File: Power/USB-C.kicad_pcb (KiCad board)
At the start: 2 copper layers, 80 x 30 mm, 40 parts, among them J1 USB_C_Receptacle_PowerOnly_6P, J2 Barrel_Jack_Switch, J3 Barrel_Jack_Switch, J4 Barrel_Jack_Switch, J5 Barrel_Jack_Switch, SW1 15v12, SW2 12v9, U1 HUSB237, U2 TPS73801, U3 TPS73801

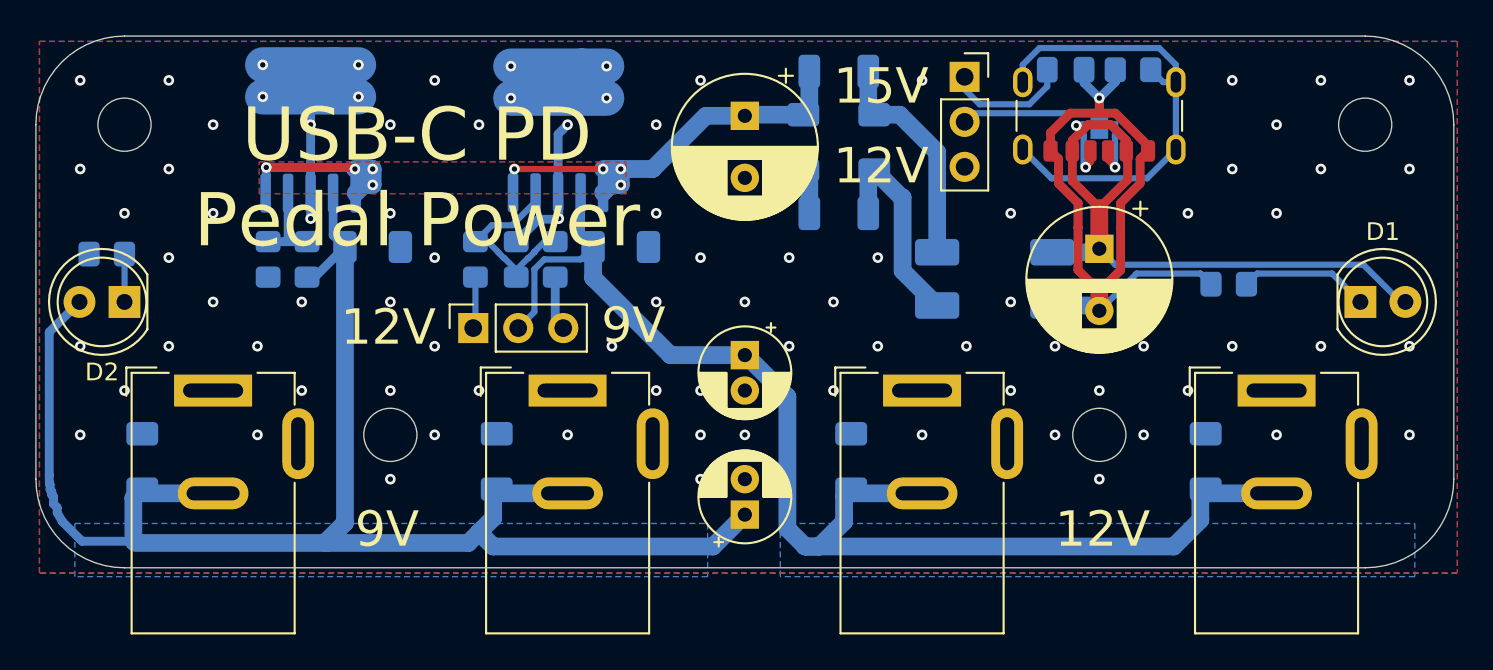
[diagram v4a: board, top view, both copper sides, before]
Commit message: USB-C power board: use the Würth reverse-mounted LEDs
This is the other board that had status lights on the non-SMD side.
Replace the through-hole LED with the reverse-mounted SMD ones.

Signed-off-by: Linus Torvalds <torvalds@linux-foundation.org>
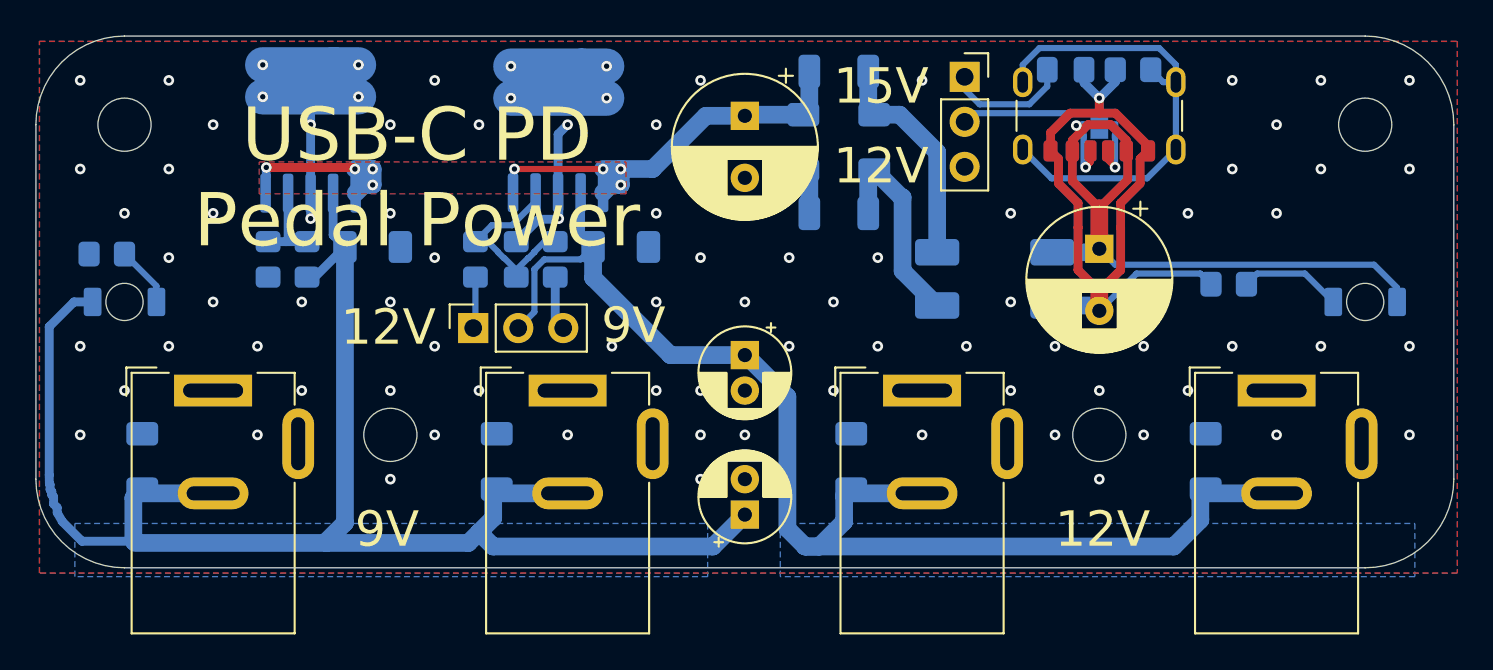
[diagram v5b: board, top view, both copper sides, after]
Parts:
- D1, D2: footprint LED_THT:LED_D5.0mm -> Mylib:Würth Reverse Mount LED; moved to B.Cu
- moved D1 0.27 mm to (125.0, 65.0)
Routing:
- net Net-(D1-K): track 7.34 -> 5.81 mm
- net +9V: track 90.4 -> 91.3 mm
- net Net-(D2-K): track 2.70 -> 3.45 mm

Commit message: Power board: move common mode choke to front
I don't do the nice 3D models, because I'm lazy and it's too much of a
hassle.  But it also means that it wasn't visually obvious that the
common mode choke ends up being very inconvenient on the back of the
board.

I'm perfectly fine with the usual low profile SMD components there, but
that choke is 3.5mm high, which is about twice as much as the other
components.

It's not that bad on the power board (which I don't have an enclosure
for anyway, although I'm looking at maybe just encasing it in resin with
a mold).  On the VGND effects board it's a non-starter.

Of course, I'm not convinced the choke actually matters, and the answer
may just be to remove it again, but until I see the effects of it let's
just move it to the front of the board.

It's going to be inconvenient to solder - I much prefer the hotplate -
but particularly on the power board I already have that USB-C connector
that I do with a hot-air station, and they are right next to each other,
so I can probably just do them together.

I'll have to think about the effects board more.  I don't actually have
room on the top of the board because I want to keep the electrolytics up
there, and keep the area in the middle clear for if I ever re-introduce
the joiner/splitter model with a third audio jack.

I think the inter-board connector there in the middle was a mistake.
It's in the way not only for this choke, but for any single-pot design
if I ever do one.

So the solution may be that I'll just have to move the connector around,
but that obviously means that I lose backwards compatibility with
existing effects boards.  Not really a big deal - unlike the enclosure
changes, it's easy enough to just do new boards - but if I make that
kind of change I want to make sure I think it through and get it right.

So let's wait to see if the choke even makes a difference.

Signed-off-by: Linus Torvalds <torvalds@linux-foundation.org>
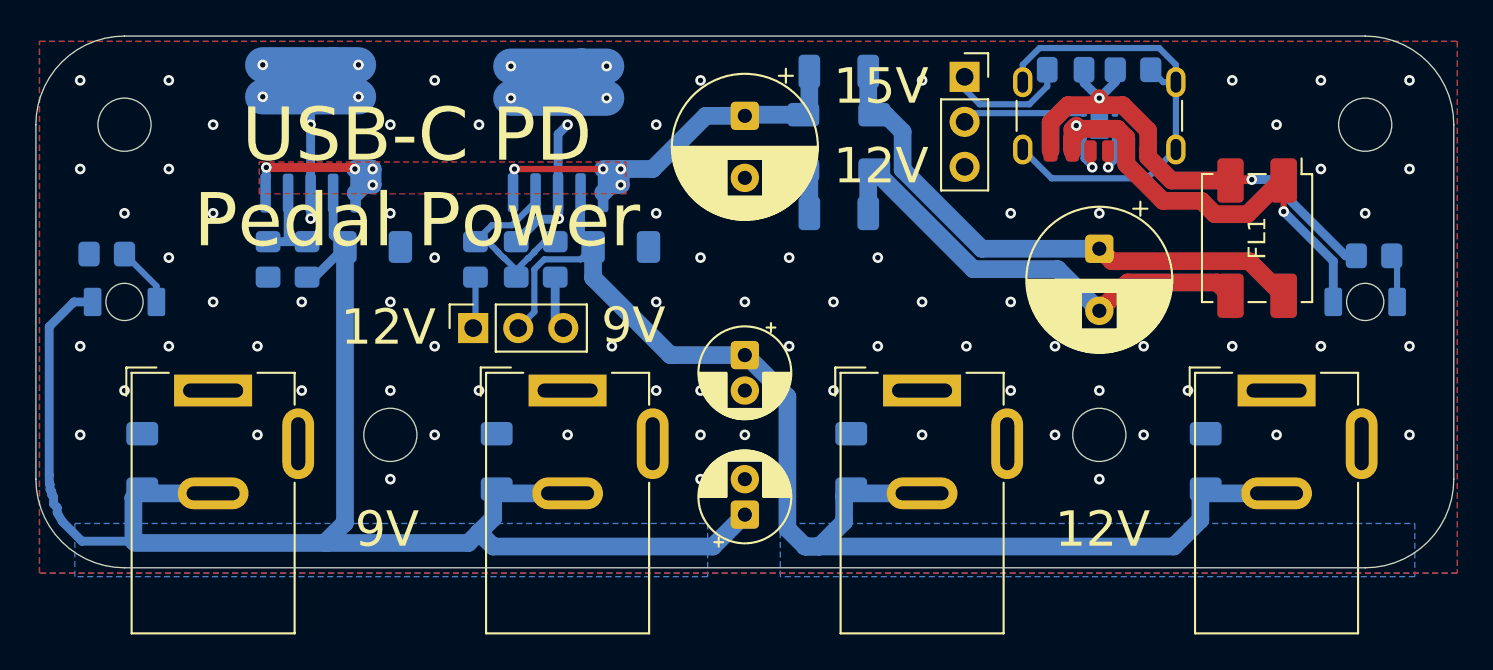
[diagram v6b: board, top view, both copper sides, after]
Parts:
- FL1: moved to F.Cu
- moved FL1 15.0 mm to (118.9, 61.4), turned to -90 degrees
- moved R1 8.35 mm to (125.5, 62.4)
- turned D1 to 180 degrees
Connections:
- C1 pad 1: VBUS -> Net-(C1-Pad1)
- C1 pad 2: GNDBUS -> Net-(C1-Pad2)
- C2 pad 1: Net-(C2-Pad1) -> Net-(C1-Pad1)
- C2 pad 2: Net-(C2-Pad2) -> Net-(C1-Pad2)
- FB1 pad 1: Net-(C2-Pad1) -> Net-(C1-Pad1)
- FB2 pad 1: Net-(C2-Pad2) -> Net-(C1-Pad2)
- FL1 pad 3: Net-(C2-Pad2) -> Net-(C1-Pad2)
- FL1 pad 4: Net-(C2-Pad1) -> Net-(C1-Pad1)
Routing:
- net Net-(C1-Pad1): track 0.00 -> 31.3 mm
- net Net-(C1-Pad2): track 0.00 -> 26.9 mm
- net GNDBUS: track 43.2 -> 29.5 mm, vias 1 -> 2
- net Net-(C2-Pad1): track 12.7 -> 0.00 mm
- net Net-(C2-Pad2): track 11.7 -> 0.00 mm
- net VBUS: track 37.1 -> 27.5 mm, vias 1 -> 2
- net Net-(D1-K): track 5.81 -> 2.72 mm
